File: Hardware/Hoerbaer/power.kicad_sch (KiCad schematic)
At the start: 49 parts, among them J12 Battery 1S Li-Ion, Q1 DMG3415UQ-7, U12 MAX17048G, U13 TPS61288, U8 MCP73831T-2ACI/OT (4.2V), U9 TPS63001

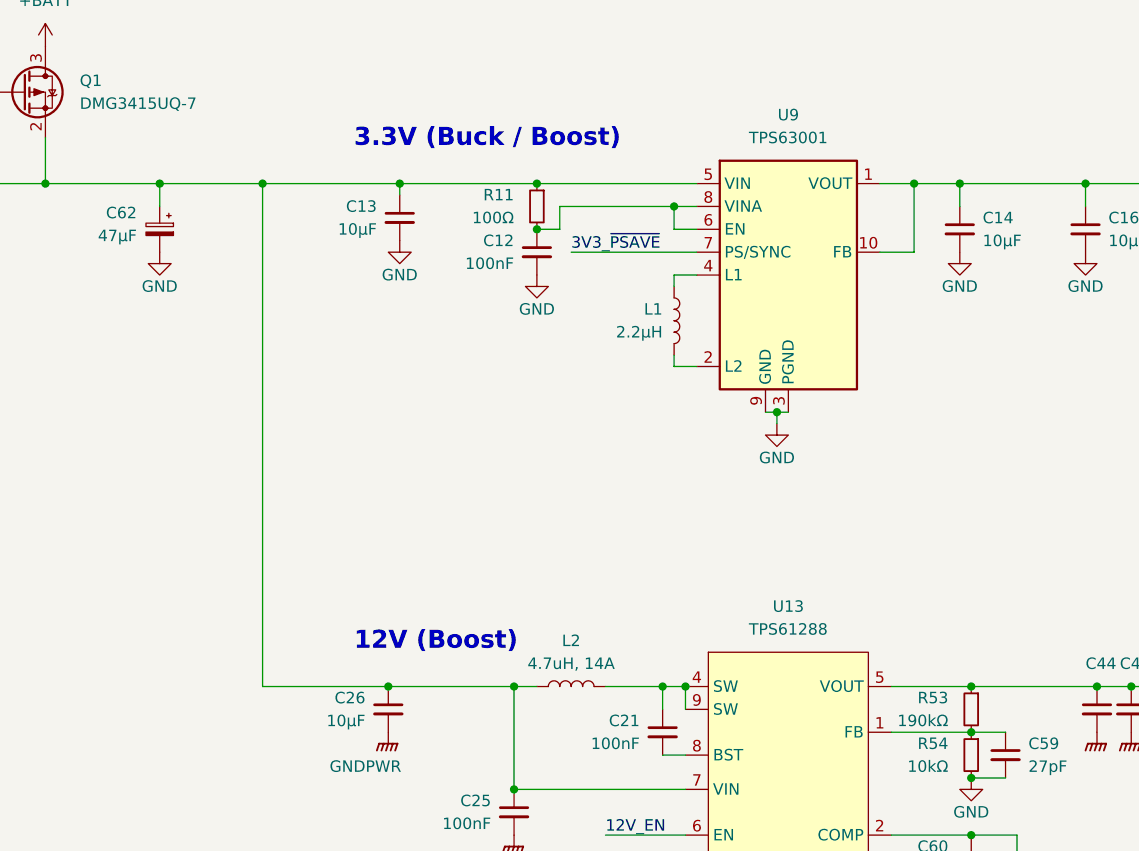
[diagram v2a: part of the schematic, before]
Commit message: More numbers, changed HBI input package, i2c addresses, layout.
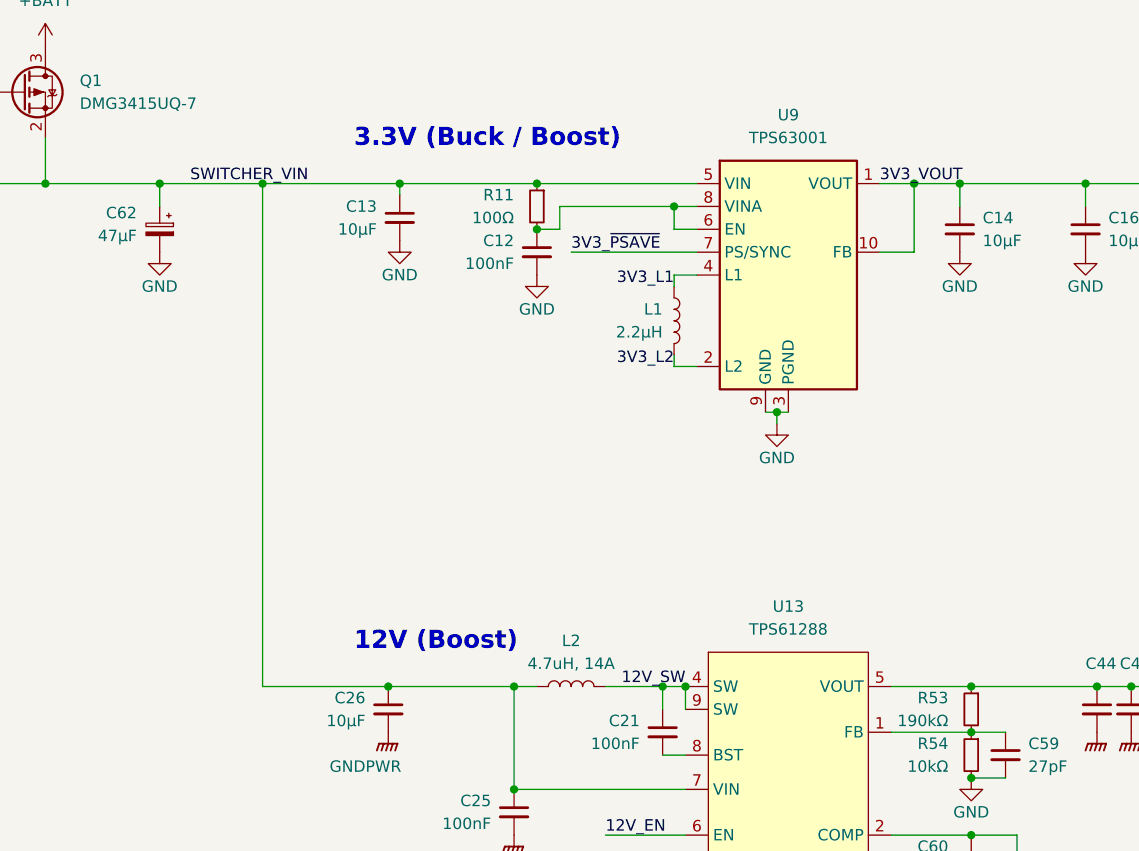
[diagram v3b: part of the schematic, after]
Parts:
- J12: footprint Connector_Wire:SolderWire-0.75sqmm_1x02_P7mm_D1.25mm_OD3.5mm -> Connector_Phoenix_MSTB:PhoenixContact_MSTBVA_2,5_2-G-5,08_1x02_P5.08mm_Vertical
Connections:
- net 3V3_L1: now reaches L1.1, U9.4 (L1)
- net 3V3_L2: now reaches L1.2, U9.2 (L2)
- net SWITCHER_VIN: now reaches C13.1, C25.1, C26.1, C62.1, D3.1 (K), L2.1, Q1.2 (S), R11.1, U13.7 (VIN), U9.5 (VIN)
- net 12V_SW: now reaches C21.1, L2.2, U13.4 (SW), U13.9 (SW)
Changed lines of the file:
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@@
+    (effects (font (size 1.27 1.27)) (justify right bottom))
+  )
+  (label "3V3_L2" (at 123.19 63.5 180) (fields_autoplaced)
     (effects (font (size 1.27 1.27)) (justify right bottom))
   )
@@
     (effects (font (size 1.27 1.27)) (justify right bottom))
   )
+  (label "3V3_L1" (at 123.19 54.61 180) (fields_autoplaced)
+    (effects (font (size 1.27 1.27)) (justify right bottom))
+  )
   (label "12V_EN" (at 115.57 115.57 0) (fields_autoplaced)
     (effects (font (size 1.27 1.27)) (justify left bottom))
@@
     (effects (font (size 1.27 1.27)) (justify left bottom))
   )
+  (label "12V_SW" (at 124.46 99.06 180) (fields_autoplaced)
+    (effects (font (size 1.27 1.27)) (justify right bottom))
+  )
+  (label "3V3_VOUT" (at 146.05 43.18 0) (fields_autoplaced)
+    (effects (font (size 1.27 1.27)) (justify left bottom))
+  )
   (label "PWR_I2C_SCL" (at 223.52 102.87 0) (fields_autoplaced)
     (effects (font (size 1.27 1.27)) (justify left bottom))
   )
   (label "BAT_~{ALRT}" (at 53.34 185.42 180) (fields_autoplaced)
+    (effects (font (size 1.27 1.27)) (justify right bottom))
+  )
+  (label "SWITCHER_VIN" (at 82.55 43.18 180) (fields_autoplaced)
     (effects (font (size 1.27 1.27)) (justify right bottom))
   )
@@
       (effects (font (size 1.27 1.27)) hide)
     )
-    (property "Datasheet" "" (at 247.65 102.87 0)
+    (property "Datasheet" "https://www.analog.com/media/en/technical-documentation/data-sheets/MAX17048-MAX17049.pdf" (at 247.65 102.87 0)
       (effects (font (size 1.27 1.27)) hide)
     )
@@
       (effects (font (size 1.27 1.27)) (justify left))
     )
-    (property "Footprint" "Connector_Wire:SolderWire-0.75sqmm_1x02_P7mm_D1.25mm_OD3.5mm" (at 250.19 142.24 0)
-      (effects (font (size 1.27 1.27)) hide)
-    )
+    (property "Footprint" "Connector_Phoenix_MSTB:PhoenixContact_MSTBVA_2,5_2-G-5,08_1x02_P5.08mm_Vertical" (at 250.19 142.24 0)
+      (effects (font (size 1.27 1.27)) hide)
+    )

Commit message: Layout drc error free
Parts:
- C60: value 1nF -> 4.7nF
- C61: value 30pF -> 27pF
- R55: value 36.6kΩ -> 47kΩ
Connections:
- net GND: now also C25.2
- net GNDPWR: no longer C25.2
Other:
- note added: "Inductor Selection (DS p.14) ... designed to work between 1.0 and 4.7 µH. 1µH smaller, 4.7µH less ripple. Audio: 4.7µH. Current: "make sure its rated current, especially the saturation current, is larger than its peak current during the operation." Calculations in "TPS61288 Calculation tool.xlsx""
- note removed: "Inductor Selection (DS p.14) ... designed to work between 1.0 and 4.7 µH. 1µH smaller, 4.7µH less ripple. Audio: 4.7µH. We assume: 2A@12V (Peak!), 3V minimal input Voltage I_{DC} = (V_{OUT} * I_{OUT}) / (V_{IN} * 0.9) I_{DC} = (12 * 2) / (3 * 0.9) = 8.88A I_{PP} = 1 / (L * (1/(V_{OUT}-V_{IN}) + 1/V_{IN}) * f_{SW}) I_{PP} = 1 / (4.7µH * (1/9 + 1/3) * 440kHz) I_{PP} = 1.088A (minimum f_{SW} for saf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"
- moved on the sheet: C61

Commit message: Order numbers
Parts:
- C12, C19, C21, C25: JLCPCB (none) -> C458949; MPN (none) -> MT15B104K160CT
- C59, C61: JLCPCB (none) -> C386133; MPN (none) -> UMK105CG270JV-F
- C60: JLCPCB (none) -> C1517770; MPN (none) -> GCM155L81H472KA37D
- U13: JLCPCB (none) -> C5219223; MPN (none) -> TPS61288RQQR
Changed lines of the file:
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@@
+      (effects (font (size 1.27 1.27)) hide)
+    )
+    (property "JLCPCB" "C386133" (at 160.02 120.65 0)
+      (effects (font (size 1.27 1.27)) hide)
+    )
+    (property "MPN" "UMK105CG270JV-F" (at 160.02 120.65 0)
       (effects (font (size 1.27 1.27)) hide)
     )
@@
     )
     (property "Datasheet" "~" (at 105.41 113.03 0)
+      (effects (font (size 1.27 1.27)) hide)
+    )
+    (property "JLCPCB" "C458949" (at 105.41 113.03 0)
+      (effects (font (size 1.27 1.27)) hide)
+    )
+    (property "MPN" "MT15B104K160CT" (at 105.41 113.03 0)
       (effects (font (size 1.27 1.27)) hide)
     )
@@
     )
     (property "Datasheet" "~" (at 107.95 50.8 0)
+      (effects (font (size 1.27 1.27)) hide)
+    )
+    (property "JLCPCB" "C458949" (at 107.95 50.8 0)
+      (effects (font (size 1.27 1.27)) hide)
+    )
+    (property "MPN" "MT15B104K160CT" (at 107.95 50.8 0)
       (effects (font (size 1.27 1.27)) hide)
     )
@@
     )
     (property "Datasheet" "https://www.ti.com/lit/ds/symlink/tps61288.pdf" (at 135.89 143.51 0)
+      (effects (font (size 1.27 1.27)) hide)
+    )
+    (property "JLCPCB" "C5219223" (at 135.89 115.57 0)
+      (effects (font (size 1.27 1.27)) hide)
+    )
+    (property "MPN" "TPS61288RQQR" (at 135.89 115.57 0)
       (effects (font (size 1.27 1.27)) hide)
     )
@@
       (effects (font (size 1.27 1.27)) hide)
     )
+    (property "JLCPCB" "C458949" (at 121.92 104.14 0)
+      (effects (font (size 1.27 1.27)) hide)
+    )
+    (property "MPN" "MT15B104K160CT" (at 121.92 104.14 0)
+      (effects (font (size 1.27 1.27)) hide)
+    )
     (pin "1")
     (pin "2")
@@
       (effects (font (size 1.27 1.27)) hide)
     )
+    (property "JLCPCB" "C1517770" (at 156.21 118.11 0)
+      (effects (font (size 1.27 1.27)) hide)
+    )
+    (property "MPN" "GCM155L81H472KA37D" (at 156.21 118.11 0)
+      (effects (font (size 1.27 1.27)) hide)
+    )
     (pin "1")
     (pin "2")
@@
       (effects (font (size 1.27 1.27)) hide)
     )
+    (property "JLCPCB" "C458949" (at 219.71 99.06 0)
+      (effects (font (size 1.27 1.27)) hide)
+    )
+    (property "MPN" "MT15B104K160CT" (at 219.71 99.06 0)
+      (effects (font (size 1.27 1.27)) hide)
+    )
     (pin "1")
     (pin "2")
@@
       (effects (font (size 1.27 1.27)) hide)
     )
+    (property "JLCPCB" "C386133" (at 160.02 106.68 0)
+      (effects (font (size 1.27 1.27)) hide)
+    )
+    (property "MPN" "UMK105CG270JV-F" (at 160.02 106.68 0)
+      (effects (font (size 1.27 1.27)) hide)
+    )

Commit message: Renamed JLCPCB attribute to LCSC (plugin search list)
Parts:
- C12, C19, C21, C25: JLCPCB C458949 -> (none); LCSC (none) -> C458949
- C13, C14, C16, C26: JLCPCB C6119932 -> (none); LCSC (none) -> C6119932
- C15, C20: JLCPCB C726581 -> (none); LCSC (none) -> C726581
- C44: JLCPCB C6120032 -> (none); LCSC (none) -> C6120032
- C55: JLCPCB C361188 -> (none); LCSC (none) -> C361188
- C59, C61: JLCPCB C386133 -> (none); LCSC (none) -> C386133
- C60: JLCPCB C1517770 -> (none); LCSC (none) -> C1517770
- C62: JLCPCB C110165 -> (none); LCSC (none) -> C110165
- D3: JLCPCB C432789 -> (none); LCSC (none) -> C432789
- L1: JLCPCB C341775 -> (none); LCSC (none) -> C341775
- L2: JLCPCB C2048059 -> (none); LCSC (none) -> C2048059
- Q1: JLCPCB C459537 -> (none); LCSC (none) -> C459537
- U12: JLCPCB C2682616 -> (none); LCSC (none) -> C2682616
- U13: JLCPCB C5219223 -> (none); LCSC (none) -> C5219223
- U8: JLCPCB C424093 -> (none); LCSC (none) -> C424093
- U9: JLCPCB C28060 -> (none); LCSC (none) -> C28060
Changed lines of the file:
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@@
       (effects (font (size 1.27 1.27)) hide)
     )
-    (property "JLCPCB" "C341775" (at 123.19 58.42 0)
+    (property "LCSC" "C341775" (at 123.19 58.42 0)
       (effects (font (size 1.27 1.27)) hide)
     )
@@
       (effects (font (size 1.27 1.27)) hide)
     )
-    (property "JLCPCB" "C386133" (at 160.02 120.65 0)
+    (property "LCSC" "C386133" (at 160.02 120.65 0)
       (effects (font (size 1.27 1.27)) hide)
     )
@@
       (effects (font (size 1.27 1.27)) hide)
     )
-    (property "JLCPCB" "C458949" (at 105.41 113.03 0)
+    (property "LCSC" "C458949" (at 105.41 113.03 0)
       (effects (font (size 1.27 1.27)) hide)
     )
@@
       (effects (font (size 1.27 1.27)) hide)
     )
-    (property "JLCPCB" "C6120032" (at 185.42 101.6 0)
+    (property "LCSC" "C6120032" (at 185.42 101.6 0)
       (effects (font (size 1.27 1.27)) hide)
     )
@@
       (effects (font (size 1.27 1.27)) hide)
     )
-    (property "JLCPCB" "C6119932" (at 91.44 101.6 0)
+    (property "LCSC" "C6119932" (at 91.44 101.6 0)
       (effects (font (size 1.27 1.27)) hide)
     )
@@
       (effects (font (size 1.27 1.27)) hide)
     )
-    (property "JLCPCB" "C6120032" (at 173.99 101.6 0)
+    (property "LCSC" "C6120032" (at 173.99 101.6 0)
       (effects (font (size 1.27 1.27)) hide)
     )
@@
       (effects (font (size 1.27 1.27)) hide)
     )
-    (property "JLCPCB" "C458949" (at 107.95 50.8 0)
+    (property "LCSC" "C458949" (at 107.95 50.8 0)
       (effects (font (size 1.27 1.27)) hide)
     )
@@
       (effects (font (size 1.27 1.27)) hide)
     )
-    (property "JLCPCB" "C6119932" (at 92.71 46.99 0)
+    (property "LCSC" "C6119932" (at 92.71 46.99 0)
       (effects (font (size 1.27 1.27)) hide)
     )
@@
       (effects (font (size 1.27 1.27)) hide)
     )
-    (property "JLCPCB" "C2682616" (at 247.65 129.54 0) (show_name)
+    (property "LCSC" "C2682616" (at 247.65 129.54 0) (show_name)
       (effects (font (size 1.27 1.27)) hide)
     )
@@
       (effects (font (size 1.27 1.27)) hide)
     )
-    (property "JLCPCB" "C5219223" (at 135.89 115.57 0)
+    (property "LCSC" "C5219223" (at 135.89 115.57 0)
       (effects (font (size 1.27 1.27)) hide)
     )
@@
       (effects (font (size 1.27 1.27)) hide)
     )
-    (property "JLCPCB" "C6120032" (at 170.18 101.6 0)
+    (property "LCSC" "C6120032" (at 170.18 101.6 0)
       (effects (font (size 1.27 1.27)) hide)
     )
@@
       (effects (font (size 1.27 1.27)) hide)
     )
-    (property "JLCPCB" "C459537" (at 50.8 33.02 0)
+    (property "LCSC" "C459537" (at 50.8 33.02 0)
       (effects (font (size 1.27 1.27)) hide)
     )
@@
       (effects (font (size 1.27 1.27)) hide)
     )
-    (property "JLCPCB" "C6120032" (at 189.23 101.6 0)
+    (property "LCSC" "C6120032" (at 189.23 101.6 0)
       (effects (font (size 1.27 1.27)) hide)
     )
@@
       (effects (font (size 1.27 1.27)) hide)
     )
-    (property "JLCPCB" "C6120032" (at 181.61 101.6 0)
+    (property "LCSC" "C6120032" (at 181.61 101.6 0)
       (effects (font (size 1.27 1.27)) hide)
     )
@@
       (effects (font (size 1.27 1.27)) hide)
     )
-    (property "JLCPCB" "C361188" (at 267.97 48.26 0)
+    (property "LCSC" "C361188" (at 267.97 48.26 0)
       (effects (font (size 1.27 1.27)) hide)
     )
@@
       (effects (font (size 1.27 1.27)) hide)
     )
-    (property "JLCPCB" "C458949" (at 121.92 104.14 0)
+    (property "LCSC" "C458949" (at 121.92 104.14 0)
       (effects (font (size 1.27 1.27)) hide)
     )
@@
       (effects (font (size 1.27 1.27)) hide)
     )
-    (property "JLCPCB" "C726581" (at 181.61 48.26 0)
+    (property "LCSC" "C726581" (at 181.61 48.26 0)
       (effects (font (size 1.27 1.27)) hide)
     )
@@
       (effects (font (size 1.27 1.27)) hide)
     )
-    (property "JLCPCB" "C424093" (at 247.65 55.88 0)
+    (property "LCSC" "C424093" (at 247.65 55.88 0)
       (effects (font (size 1.27 1.27)) hide)
     )
@@
       (effects (font (size 1.27 1.27)) hide)
     )
-    (property "JLCPCB" "C1517770" (at 156.21 118.11 0)
+    (property "LCSC" "C1517770" (at 156.21 118.11 0)
       (effects (font (size 1.27 1.27)) hide)
     )
@@
       (effects (font (size 1.27 1.27)) hide)
     )
-    (property "JLCPCB" "C6119932" (at 154.94 48.26 0)
+    (property "LCSC" "C6119932" (at 154.94 48.26 0)
       (effects (font (size 1.27 1.27)) hide)
     )
@@
       (effects (font (size 1.27 1.27)) hide)
     )
-    (property "JLCPCB" "C458949" (at 219.71 99.06 0)
+    (property "LCSC" "C458949" (at 219.71 99.06 0)
       (effects (font (size 1.27 1.27)) hide)
     )
@@
       (effects (font (size 1.27 1.27)) hide)
     )
-    (property "JLCPCB" "C6120032" (at 177.8 101.6 0)
+    (property "LCSC" "C6120032" (at 177.8 101.6 0)
       (effects (font (size 1.27 1.27)) hide)
     )
@@
       (effects (font (size 1.27 1.27)) hide)
     )
-    (property "JLCPCB" "C432789" (at 44.45 43.18 0)
+    (property "LCSC" "C432789" (at 44.45 43.18 0)
       (effects (font (size 1.27 1.27)) hide)
     )
@@
       (effects (font (size 1.27 1.27)) hide)
     )
-    (property "JLCPCB" "C110165" (at 66.04 48.26 0)
+    (property "LCSC" "C110165" (at 66.04 48.26 0)
       (effects (font (size 1.27 1.27)) hide)
     )
@@
       (effects (font (size 1.27 1.27)) hide)
     )
-    (property "JLCPCB" "C386133" (at 160.02 106.68 0)
+    (property "LCSC" "C386133" (at 160.02 106.68 0)
       (effects (font (size 1.27 1.27)) hide)
     )
@@
       (effects (font (size 1.27 1.27)) hide)
     )
-    (property "JLCPCB" "C2048059" (at 111.76 99.06 90)
+    (property "LCSC" "C2048059" (at 111.76 99.06 90)
       (effects (font (size 1.27 1.27)) hide)
     )
@@
       (effects (font (size 1.27 1.27)) hide)
     )
-    (property "JLCPCB" "C361188" (at 219.71 48.26 0)
+    (property "LCSC" "C361188" (at 219.71 48.26 0)
       (effects (font (size 1.27 1.27)) hide)
     )
@@
       (effects (font (size 1.27 1.27)) hide)
     )
-    (property "JLCPCB" "C726581" (at 121.92 123.19 0)
+    (property "LCSC" "C726581" (at 121.92 123.19 0)
       (effects (font (size 1.27 1.27)) hide)
     )
@@
       (effects (font (size 1.27 1.27)) hide)
     )
-    (property "JLCPCB" "C28060" (at 135.89 53.34 0)
+    (property "LCSC" "C28060" (at 135.89 53.34 0)
       (effects (font (size 1.27 1.27)) hide)
     )
@@
       (effects (font (size 1.27 1.27)) hide)
     )
-    (property "JLCPCB" "C6119932" (at 168.91 48.26 0)
-      (effects (font (size 1.27 1.27)) hide)
-    )
+    (property "LCSC" "C6119932" (at 168.91 48.26 0)
+      (effects (font (size 1.27 1.27)) hide)
+    )
